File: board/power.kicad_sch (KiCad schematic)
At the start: 32 parts

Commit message: Fix 1.1V regulator reference
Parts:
- SW_REG2: JLC WLCSP-20(1.6x2) -> TSOT-23-6; LCSC C603207 -> C2650336
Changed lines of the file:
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@@
 			)
 		)
-		(property "JLC" "WLCSP-20(1.6x2) "
+		(property "JLC" "TSOT-23-6"
 			(at 106.68 49.53 0)
 			(effects
@@
 			)
 		)
-		(property "LCSC" "C603207"
+		(property "LCSC" "C2650336"
 			(at 106.68 49.53 0)
 			(effects

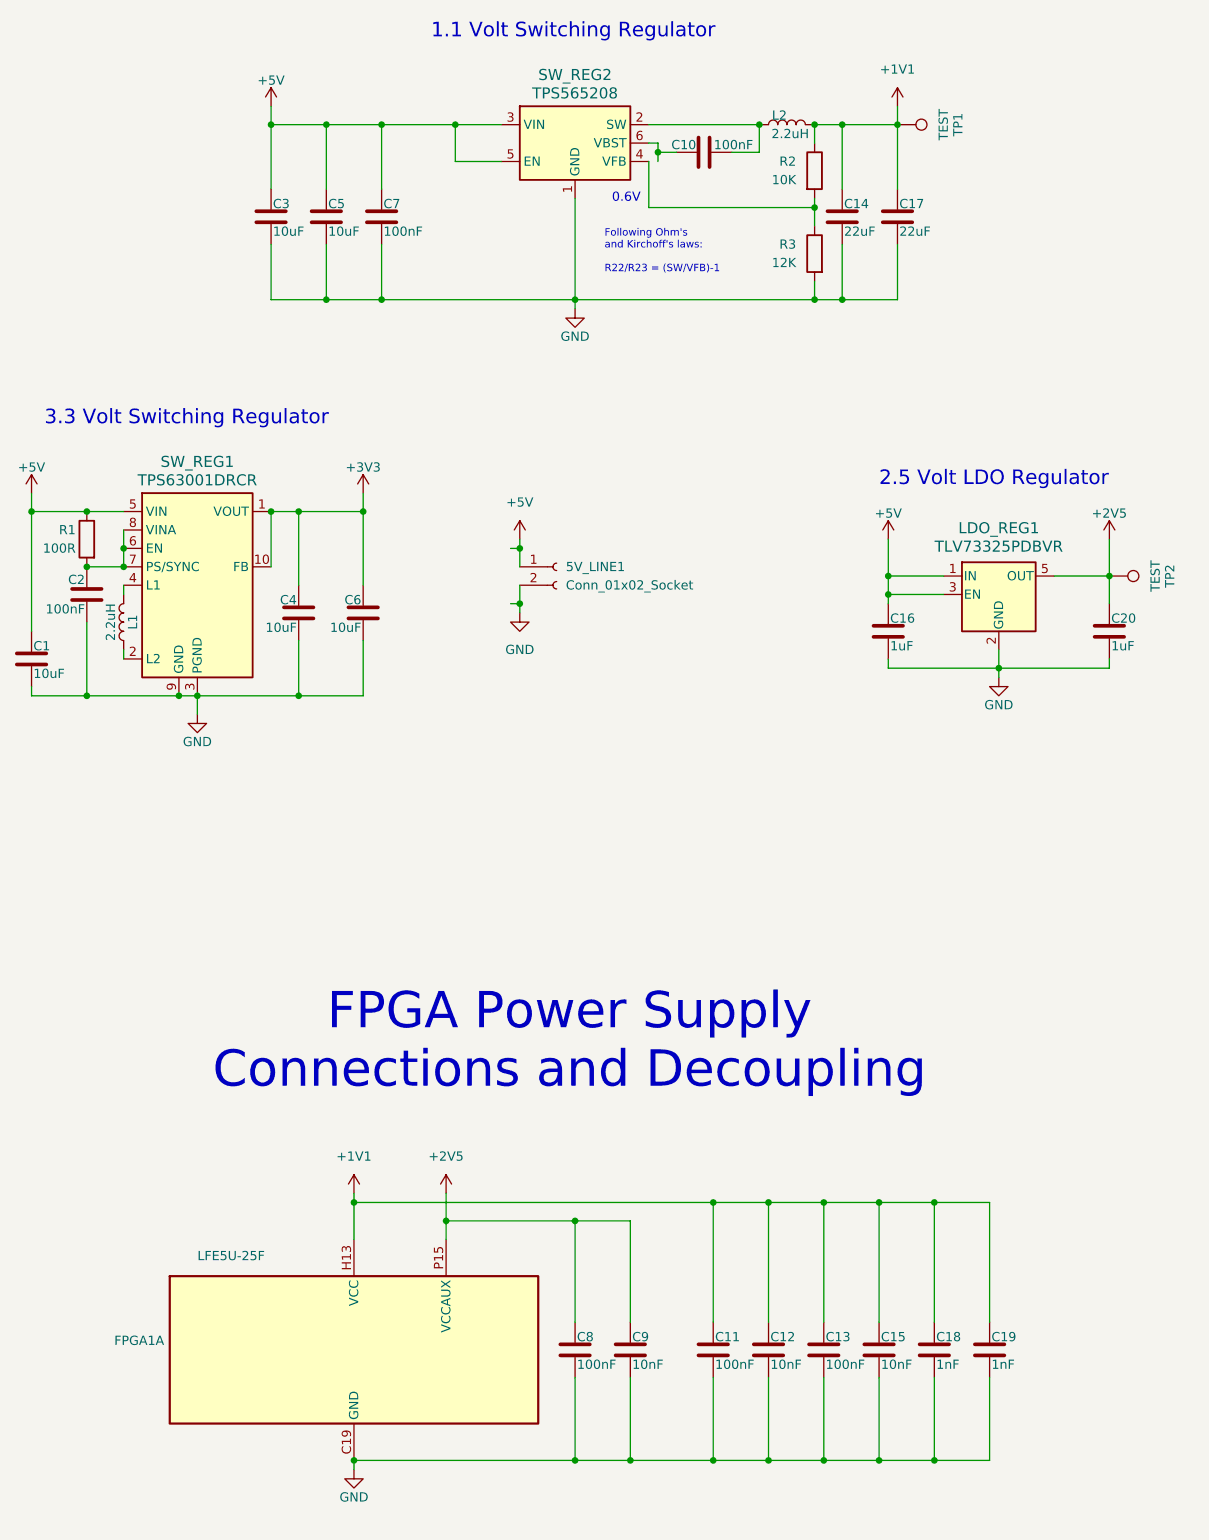
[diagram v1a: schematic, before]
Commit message: Change LFE5U chip from BGA381 to BGA256 package
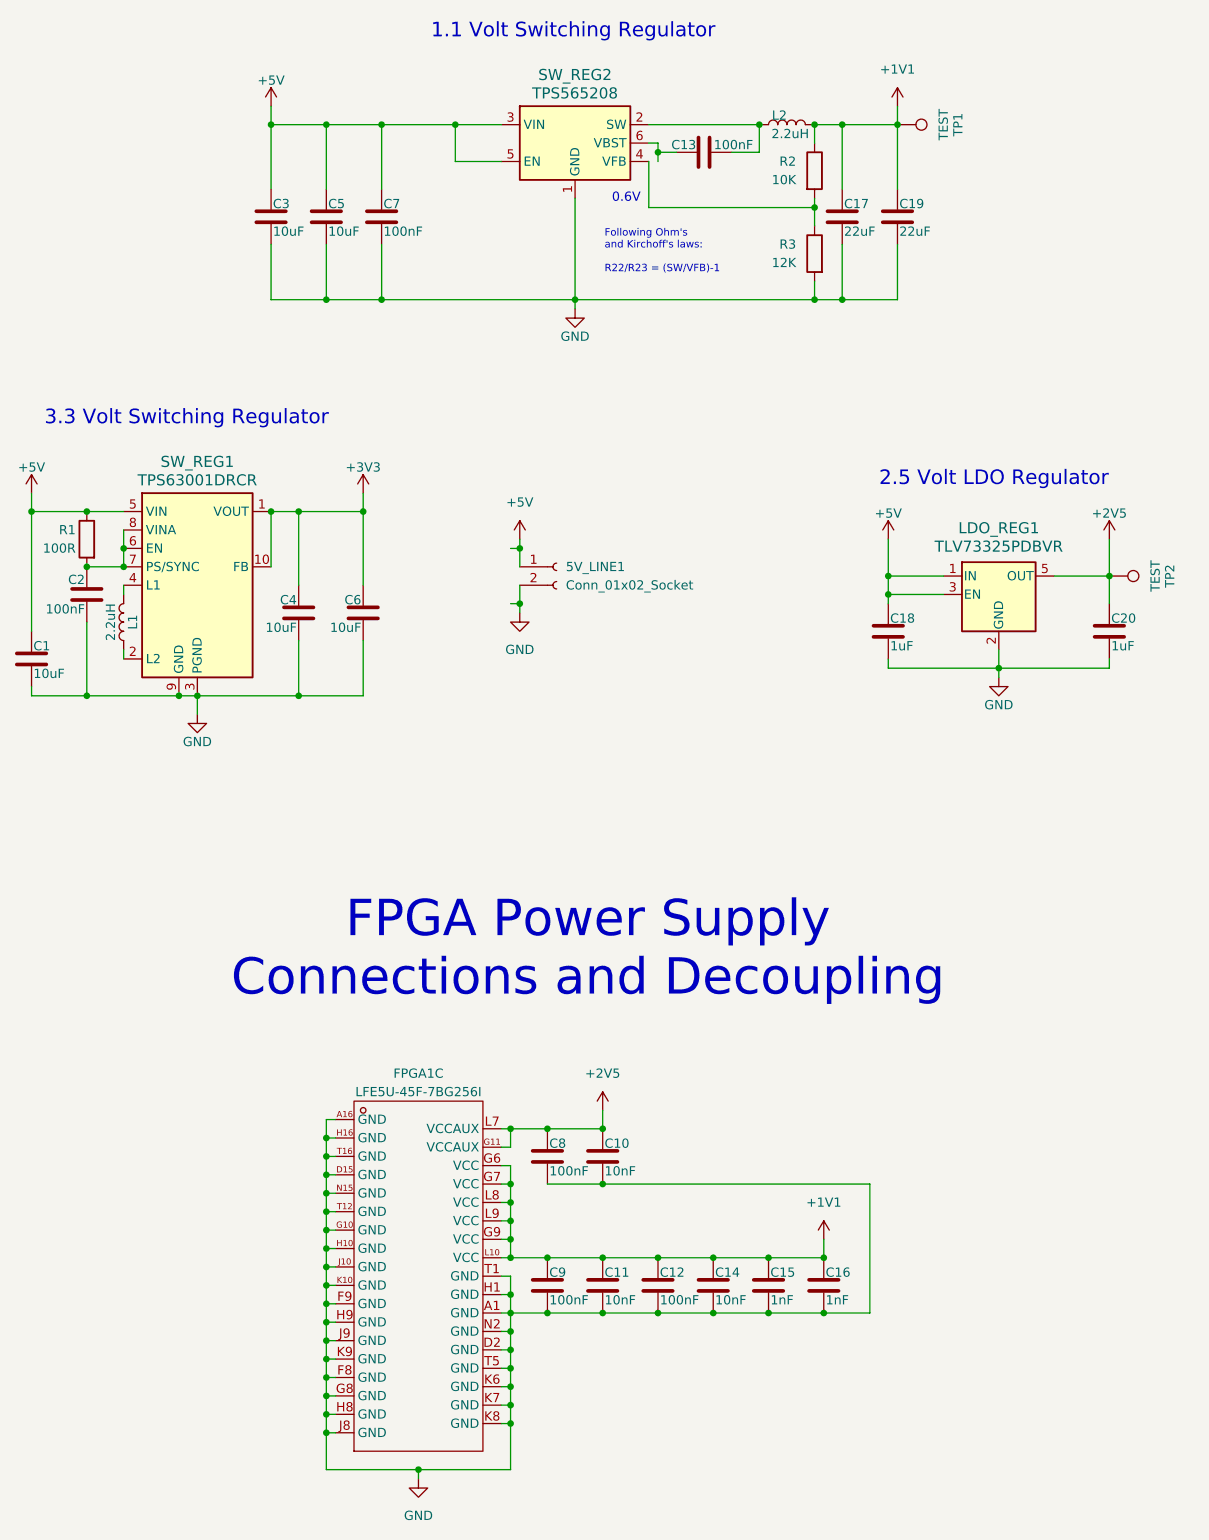
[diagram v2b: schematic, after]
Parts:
- removed FPGA1: LFE5U-25F, Package_BGA:Lattice_caBGA-381_17.0x17.0mm_Layout20x20_P0.8mm_Ball0.4mm_Pad0.4mm_NSMD, symbol FPGA_Lattice:LFE5U-85F-8BG381x
- added FPGA1: LFE5U-45F-7BG256I, HispalisFPGA:CABGA-256_L14.0-W14.0-R16-C16-P0.80-TL, symbol LFE5U-45F-7BG256I:LFE5U-45F-7BG256I
- renumbered C9 to C10, C12 to C11, C13 to C12, C10 to C13, C15 to C14, C18 to C15, C19 to C16, C14 to C17, C16 to C18, C17 to C19, C11 to C9
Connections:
- net +1V1: now also FPGA1.G6 (VCC), FPGA1.G7 (VCC), FPGA1.G9 (VCC), FPGA1.L10 (VCC), FPGA1.L8 (VCC), FPGA1.L9 (VCC)
- net +2V5: now also FPGA1.G11 (VCCAUX), FPGA1.L7 (VCCAUX)
- net GND: now also FPGA1.A1 (GND), FPGA1.A16 (GND), FPGA1.D15 (GND), FPGA1.D2 (GND), FPGA1.F8 (GND), FPGA1.F9 (GND), FPGA1.G10 (GND), FPGA1.G8 (GND), FPGA1.H1 (GND), FPGA1.H10 (GND), FPGA1.H16 (GND), FPGA1.H8 (GND), FPGA1.H9 (GND), FPGA1.J10 (GND), FPGA1.J8 (GND), FPGA1.J9 (GND), FPGA1.K10 (GND), FPGA1.K6 (GND), FPGA1.K7 (GND), FPGA1.K8 (GND), FPGA1.K9 (GND), FPGA1.N15 (GND), FPGA1.N2 (GND), FPGA1.T1 (GND), FPGA1.T12 (GND), FPGA1.T16 (GND), FPGA1.T5 (GND)
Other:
- moved on the sheet: C10, C11, C12, C14, C15, C16, C8, C9
